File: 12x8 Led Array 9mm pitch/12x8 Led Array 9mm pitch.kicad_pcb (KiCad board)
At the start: 4 copper layers, 195 x 131.8 mm, 313 parts, among them J1 LED ch 1-24, J2 LED ch 25-48, J3 LED ch 49-72, J4 LED ch 73-96, J5 logic/analog, U1 CD74HC4067M96, U2 CD74HC4067M96, U3 CD74HC4067M96, U4 CD74HC4067M96, U5 CD74HC4067M96, U6 CD74HC4067M96

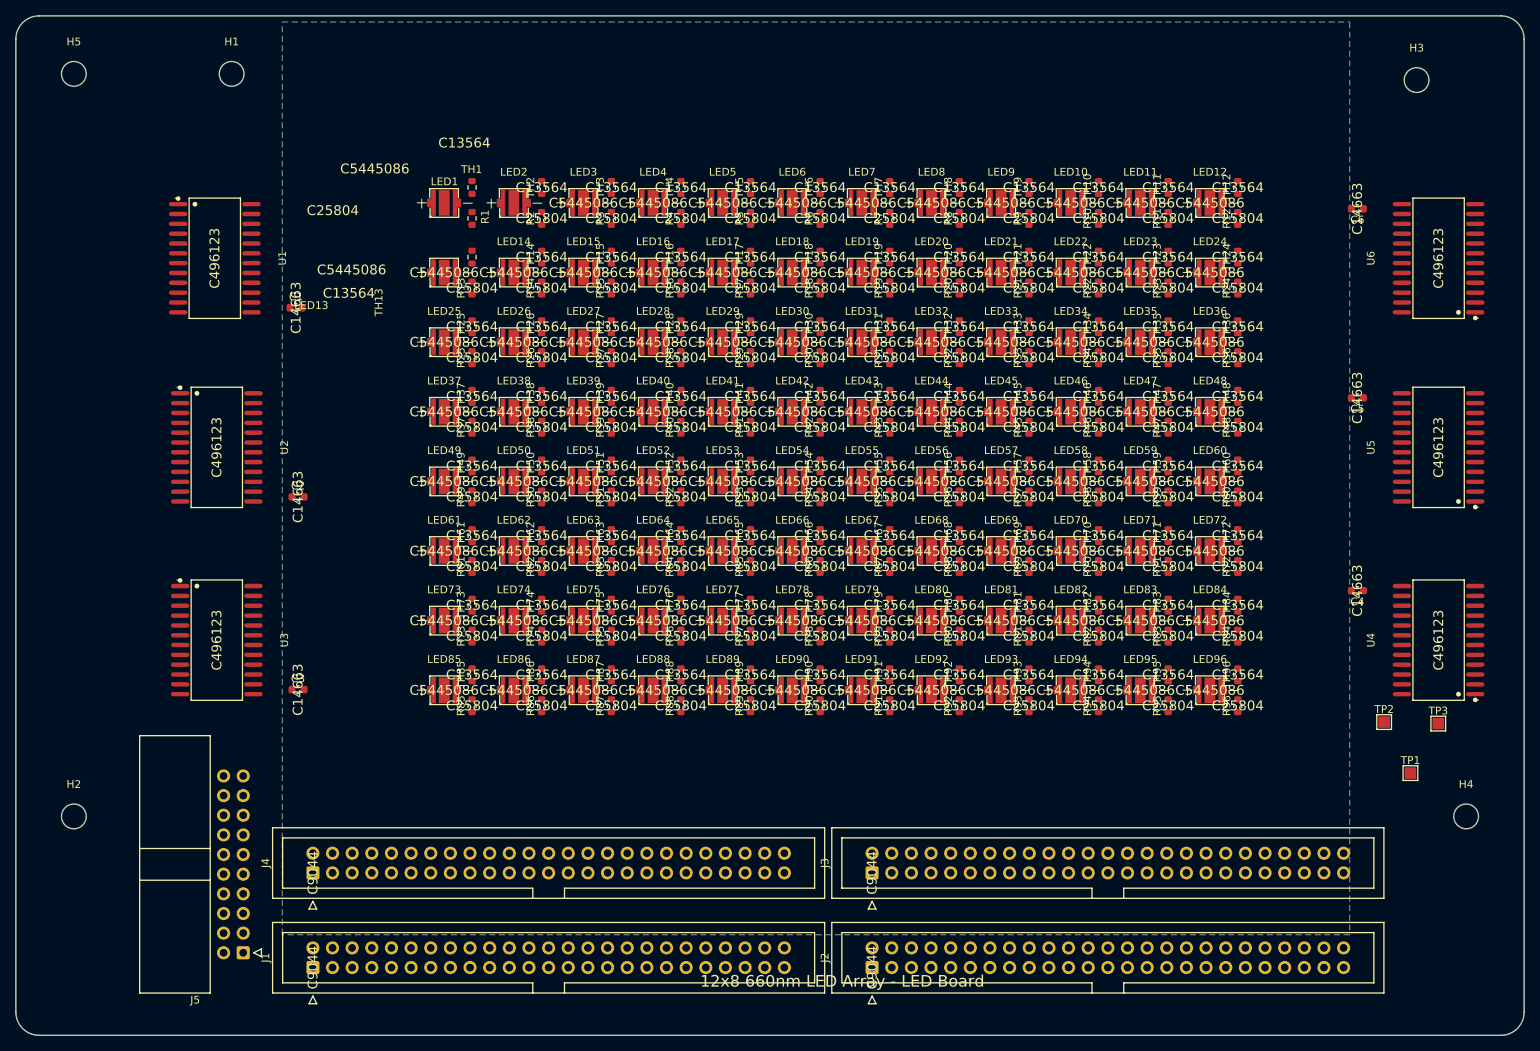
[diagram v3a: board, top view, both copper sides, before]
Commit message: Pull mux strips in (board now 190x131.8mm), thermal via farms + fills
- U1-U3/C1-C3 +5mm, U4-U6/C4-C6 -5mm; outline redrawn; H4 -> (227,128)
- 480 thermal vias (0.3/0.6mm, 5 per LED pad 3, cathode nets)
- 96 B.Cu cathode islands (6.5mm, solid connect, priority 2) + GND
  planes on In1/In2/B.Cu resized to new outline and filled
- PCB nets refreshed from the FIXED schematic netlist (board still
  carried the pre-fix merged +3.3V/GND net; GND net recreated,
  1051 pads re-netted, vias + zones re-assigned)

Co-Authored-By: Claude Fable 5 <noreply@anthropic.com>
Claude-Session: https://claude.ai/code/session_017oD54uh7Tvu54u9NPQNcZB
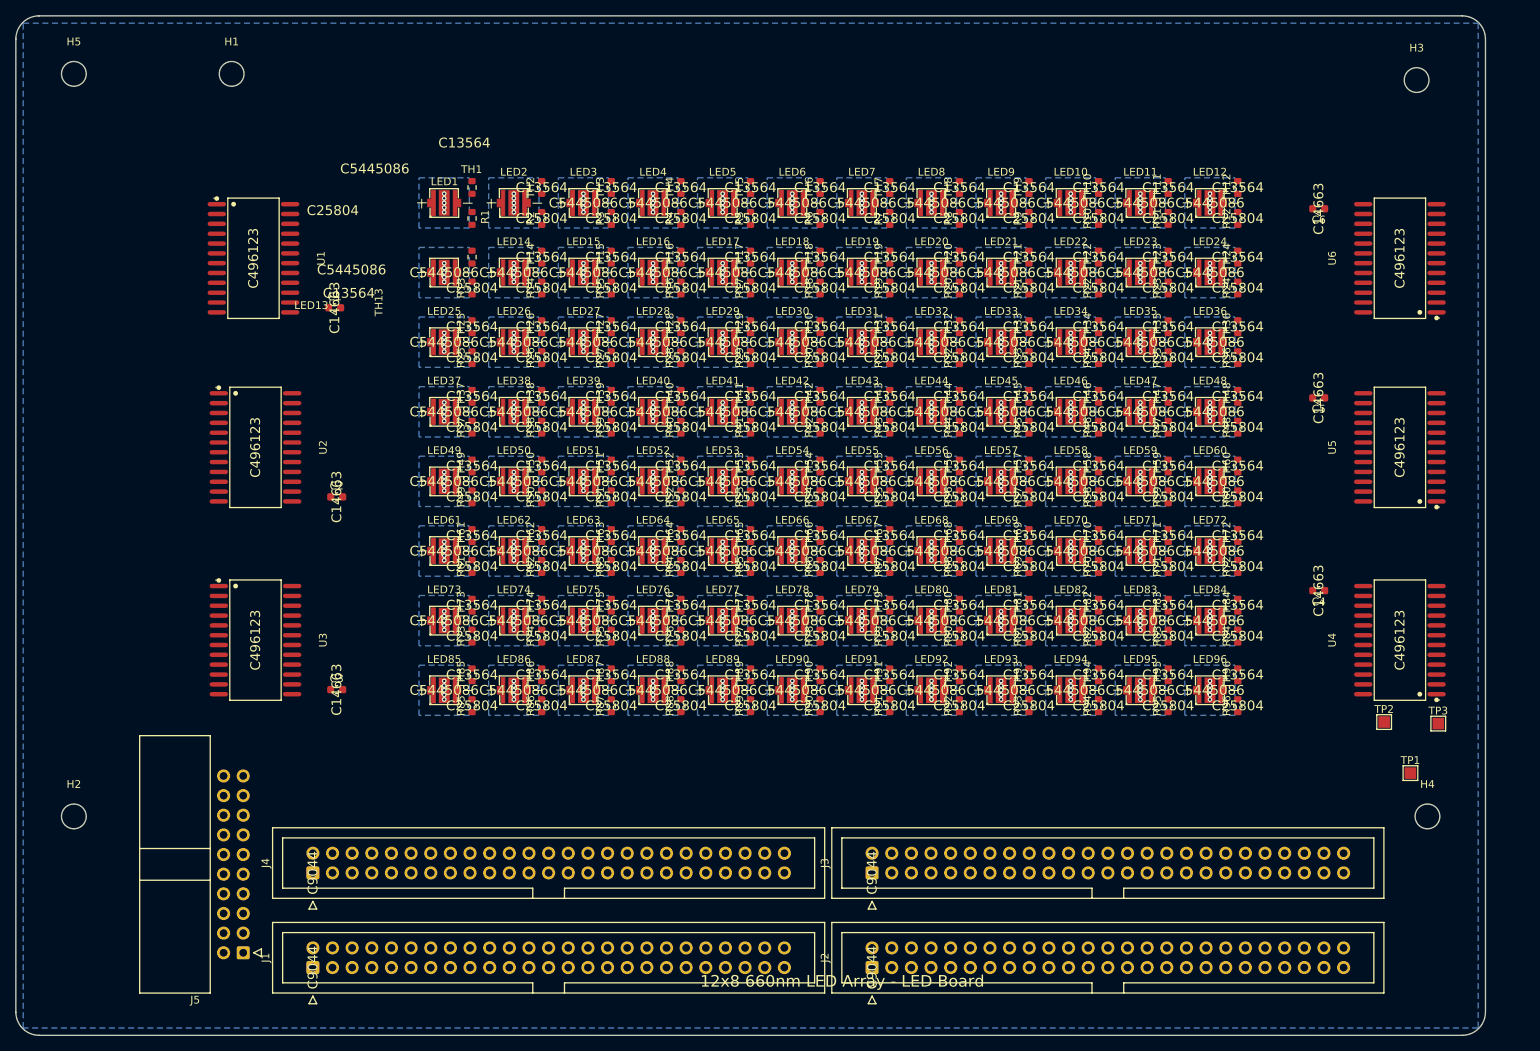
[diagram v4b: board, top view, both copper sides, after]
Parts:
- moved C1 5.00 mm to (85.7, 62.2)
- moved C2 5.00 mm to (86.0, 86.7)
- moved C3 5.00 mm to (86.0, 111.6)
- moved C4 5.00 mm to (212.9, 98.8)
- moved C5 5.00 mm to (212.9, 73.9)
- moved C6 5.00 mm to (212.9, 49.4)
- moved H4 5.00 mm to (227.0, 128.0)
- moved U1 5.00 mm to (75.2, 55.8)
- moved U2 5.00 mm to (75.5, 80.3)
- moved U3 5.00 mm to (75.5, 105.2)
- moved U4 5.00 mm to (223.4, 105.2)
- moved U5 5.00 mm to (223.4, 80.3)
- moved U6 5.00 mm to (223.4, 55.8)
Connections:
- C1 pad 2: +3.3V -> GND
- C2 pad 2: +3.3V -> GND
- C3 pad 2: +3.3V -> GND
- C4 pad 2: +3.3V -> GND
- C5 pad 2: +3.3V -> GND
- C6 pad 2: +3.3V -> GND
- J1 pad 10: /LED_K5 -> /LED_K2
- J1 pad 11: /LED_A6 -> /LED_A14
- J1 pad 12: /LED_K6 -> /LED_K14
- J1 pad 13: /LED_A7 -> /LED_A26
- J1 pad 14: /LED_K7 -> /LED_K26
- J1 pad 15: /LED_A8 -> /LED_A38
- J1 pad 16: /LED_K8 -> /LED_K38
- J1 pad 17: /LED_A9 -> /LED_A3
- J1 pad 18: /LED_K9 -> /LED_K3
- J1 pad 19: /LED_A10 -> /LED_A15
- J1 pad 20: /LED_K10 -> /LED_K15
- J1 pad 21: /LED_A11 -> /LED_A27
- J1 pad 22: /LED_K11 -> /LED_K27
- J1 pad 23: /LED_A12 -> /LED_A39
- J1 pad 24: /LED_K12 -> /LED_K39
- J1 pad 25: /LED_A13 -> /LED_A4
- J1 pad 26: /LED_K13 -> /LED_K4
- J1 pad 27: /LED_A14 -> /LED_A16
- J1 pad 28: /LED_K14 -> /LED_K16
- J1 pad 29: /LED_A15 -> /LED_A28
- J1 pad 3: /LED_A2 -> /LED_A13
- J1 pad 30: /LED_K15 -> /LED_K28
- J1 pad 31: /LED_A16 -> /LED_A40
- J1 pad 32: /LED_K16 -> /LED_K40
- J1 pad 33: /LED_A17 -> /LED_A5
- J1 pad 34: /LED_K17 -> /LED_K5
- J1 pad 35: /LED_A18 -> /LED_A17
- J1 pad 36: /LED_K18 -> /LED_K17
- J1 pad 37: /LED_A19 -> /LED_A29
- J1 pad 38: /LED_K19 -> /LED_K29
- J1 pad 39: /LED_A20 -> /LED_A41
- J1 pad 4: /LED_K2 -> /LED_K13
- J1 pad 40: /LED_K20 -> /LED_K41
- J1 pad 41: /LED_A21 -> /LED_A6
- J1 pad 42: /LED_K21 -> /LED_K6
- J1 pad 43: /LED_A22 -> /LED_A18
- J1 pad 44: /LED_K22 -> /LED_K18
- J1 pad 45: /LED_A23 -> /LED_A30
- J1 pad 46: /LED_K23 -> /LED_K30
- J1 pad 47: /LED_A24 -> /LED_A42
- J1 pad 48: /LED_K24 -> /LED_K42
- J1 pad 49: +3.3V -> GND
- J1 pad 5: /LED_A3 -> /LED_A25
- J1 pad 50: +3.3V -> GND
- J1 pad 6: /LED_K3 -> /LED_K25
- J1 pad 7: /LED_A4 -> /LED_A37
- J1 pad 8: /LED_K4 -> /LED_K37
- J1 pad 9: /LED_A5 -> /LED_A2
- J2 pad 1: /LED_A25 -> /LED_A7
- J2 pad 10: /LED_K29 -> /LED_K8
- J2 pad 11: /LED_A30 -> /LED_A20
- J2 pad 12: /LED_K30 -> /LED_K20
- J2 pad 13: /LED_A31 -> /LED_A32
- J2 pad 14: /LED_K31 -> /LED_K32
- J2 pad 15: /LED_A32 -> /LED_A44
- J2 pad 16: /LED_K32 -> /LED_K44
- J2 pad 17: /LED_A33 -> /LED_A9
- J2 pad 18: /LED_K33 -> /LED_K9
- J2 pad 19: /LED_A34 -> /LED_A21
- J2 pad 2: /LED_K25 -> /LED_K7
- J2 pad 20: /LED_K34 -> /LED_K21
- J2 pad 21: /LED_A35 -> /LED_A33
- J2 pad 22: /LED_K35 -> /LED_K33
- J2 pad 23: /LED_A36 -> /LED_A45
- J2 pad 24: /LED_K36 -> /LED_K45
- J2 pad 25: /LED_A37 -> /LED_A10
- J2 pad 26: /LED_K37 -> /LED_K10
- J2 pad 27: /LED_A38 -> /LED_A22
- J2 pad 28: /LED_K38 -> /LED_K22
- J2 pad 29: /LED_A39 -> /LED_A34
- J2 pad 3: /LED_A26 -> /LED_A19
- J2 pad 30: /LED_K39 -> /LED_K34
- J2 pad 31: /LED_A40 -> /LED_A46
- J2 pad 32: /LED_K40 -> /LED_K46
- J2 pad 33: /LED_A41 -> /LED_A11
- J2 pad 34: /LED_K41 -> /LED_K11
- J2 pad 35: /LED_A42 -> /LED_A23
- J2 pad 36: /LED_K42 -> /LED_K23
- J2 pad 37: /LED_A43 -> /LED_A35
- J2 pad 38: /LED_K43 -> /LED_K35
- J2 pad 39: /LED_A44 -> /LED_A47
- J2 pad 4: /LED_K26 -> /LED_K19
- J2 pad 40: /LED_K44 -> /LED_K47
- J2 pad 41: /LED_A45 -> /LED_A12
- J2 pad 42: /LED_K45 -> /LED_K12
- J2 pad 43: /LED_A46 -> /LED_A24
- J2 pad 44: /LED_K46 -> /LED_K24
- J2 pad 45: /LED_A47 -> /LED_A36
- J2 pad 46: /LED_K47 -> /LED_K36
- J2 pad 49: +3.3V -> GND
- J2 pad 5: /LED_A27 -> /LED_A31
- J2 pad 50: +3.3V -> GND
- J2 pad 6: /LED_K27 -> /LED_K31
- J2 pad 7: /LED_A28 -> /LED_A43
- J2 pad 8: /LED_K28 -> /LED_K43
- J2 pad 9: /LED_A29 -> /LED_A8
- J3 pad 1: /LED_A49 -> /LED_A55
- J3 pad 10: /LED_K53 -> /LED_K56
- J3 pad 11: /LED_A54 -> /LED_A68
- J3 pad 12: /LED_K54 -> /LED_K68
- J3 pad 13: /LED_A55 -> /LED_A80
- J3 pad 14: /LED_K55 -> /LED_K80
- J3 pad 15: /LED_A56 -> /LED_A92
- J3 pad 16: /LED_K56 -> /LED_K92
- J3 pad 19: /LED_A58 -> /LED_A69
- J3 pad 2: /LED_K49 -> /LED_K55
- J3 pad 20: /LED_K58 -> /LED_K69
- J3 pad 21: /LED_A59 -> /LED_A81
- J3 pad 22: /LED_K59 -> /LED_K81
- J3 pad 23: /LED_A60 -> /LED_A93
- J3 pad 24: /LED_K60 -> /LED_K93
- J3 pad 25: /LED_A61 -> /LED_A58
- J3 pad 26: /LED_K61 -> /LED_K58
- J3 pad 27: /LED_A62 -> /LED_A70
- J3 pad 28: /LED_K62 -> /LED_K70
- J3 pad 29: /LED_A63 -> /LED_A82
- J3 pad 3: /LED_A50 -> /LED_A67
- J3 pad 30: /LED_K63 -> /LED_K82
- J3 pad 31: /LED_A64 -> /LED_A94
- J3 pad 32: /LED_K64 -> /LED_K94
- J3 pad 33: /LED_A65 -> /LED_A59
- J3 pad 34: /LED_K65 -> /LED_K59
- J3 pad 35: /LED_A66 -> /LED_A71
- J3 pad 36: /LED_K66 -> /LED_K71
- J3 pad 37: /LED_A67 -> /LED_A83
- J3 pad 38: /LED_K67 -> /LED_K83
- J3 pad 39: /LED_A68 -> /LED_A95
- J3 pad 4: /LED_K50 -> /LED_K67
- J3 pad 40: /LED_K68 -> /LED_K95
- J3 pad 41: /LED_A69 -> /LED_A60
- J3 pad 42: /LED_K69 -> /LED_K60
- J3 pad 43: /LED_A70 -> /LED_A72
- J3 pad 44: /LED_K70 -> /LED_K72
- J3 pad 45: /LED_A71 -> /LED_A84
- J3 pad 46: /LED_K71 -> /LED_K84
- J3 pad 47: /LED_A72 -> /LED_A96
- J3 pad 48: /LED_K72 -> /LED_K96
- J3 pad 49: +3.3V -> GND
- J3 pad 5: /LED_A51 -> /LED_A79
- J3 pad 50: +3.3V -> GND
- J3 pad 6: /LED_K51 -> /LED_K79
- J3 pad 7: /LED_A52 -> /LED_A91
- J3 pad 8: /LED_K52 -> /LED_K91
- J3 pad 9: /LED_A53 -> /LED_A56
- J4 pad 1: /LED_A73 -> /LED_A49
- J4 pad 10: /LED_K77 -> /LED_K50
- J4 pad 11: /LED_A78 -> /LED_A62
- J4 pad 12: /LED_K78 -> /LED_K62
- J4 pad 13: /LED_A79 -> /LED_A74
- J4 pad 14: /LED_K79 -> /LED_K74
- J4 pad 15: /LED_A80 -> /LED_A86
- J4 pad 16: /LED_K80 -> /LED_K86
- J4 pad 17: /LED_A81 -> /LED_A51
- J4 pad 18: /LED_K81 -> /LED_K51
- J4 pad 19: /LED_A82 -> /LED_A63
- J4 pad 2: /LED_K73 -> /LED_K49
- J4 pad 20: /LED_K82 -> /LED_K63
- J4 pad 21: /LED_A83 -> /LED_A75
- J4 pad 22: /LED_K83 -> /LED_K75
- J4 pad 23: /LED_A84 -> /LED_A87
- J4 pad 24: /LED_K84 -> /LED_K87
- J4 pad 25: /LED_A85 -> /LED_A52
- J4 pad 26: /LED_K85 -> /LED_K52
- J4 pad 27: /LED_A86 -> /LED_A64
- J4 pad 28: /LED_K86 -> /LED_K64
- J4 pad 29: /LED_A87 -> /LED_A76
- J4 pad 3: /LED_A74 -> /LED_A61
- J4 pad 30: /LED_K87 -> /LED_K76
- J4 pad 33: /LED_A89 -> /LED_A53
- J4 pad 34: /LED_K89 -> /LED_K53
- J4 pad 35: /LED_A90 -> /LED_A65
- J4 pad 36: /LED_K90 -> /LED_K65
- J4 pad 37: /LED_A91 -> /LED_A77
- J4 pad 38: /LED_K91 -> /LED_K77
- J4 pad 39: /LED_A92 -> /LED_A89
- J4 pad 4: /LED_K74 -> /LED_K61
- J4 pad 40: /LED_K92 -> /LED_K89
- J4 pad 41: /LED_A93 -> /LED_A54
- J4 pad 42: /LED_K93 -> /LED_K54
- J4 pad 43: /LED_A94 -> /LED_A66
- J4 pad 44: /LED_K94 -> /LED_K66
- J4 pad 45: /LED_A95 -> /LED_A78
- J4 pad 46: /LED_K95 -> /LED_K78
- J4 pad 47: /LED_A96 -> /LED_A90
- J4 pad 48: /LED_K96 -> /LED_K90
- J4 pad 49: +3.3V -> GND
- J4 pad 5: /LED_A75 -> /LED_A73
- J4 pad 50: +3.3V -> GND
- J4 pad 6: /LED_K75 -> /LED_K73
- J4 pad 7: /LED_A76 -> /LED_A85
- J4 pad 8: /LED_K76 -> /LED_K85
- J4 pad 9: /LED_A77 -> /LED_A50
- J5 pad 10: +3.3V -> GND
- J5 pad 12: +3.3V -> GND
- J5 pad 14: +3.3V -> GND
- J5 pad 19: +3.3V -> GND
- J5 pad 2: +3.3V -> GND
- J5 pad 20: +3.3V -> GND
- J5 pad 4: +3.3V -> GND
- J5 pad 6: +3.3V -> GND
- J5 pad 8: +3.3V -> GND
- R1 pad 2: +3.3V -> GND
- R10 pad 2: +3.3V -> GND
- R11 pad 2: +3.3V -> GND
- R12 pad 2: +3.3V -> GND
- R13 pad 2: +3.3V -> GND
- R14 pad 2: +3.3V -> GND
- R15 pad 2: +3.3V -> GND
- R16 pad 2: +3.3V -> GND
- R17 pad 2: +3.3V -> GND
- R18 pad 2: +3.3V -> GND
- R19 pad 2: +3.3V -> GND
- R2 pad 2: +3.3V -> GND
- R20 pad 2: +3.3V -> GND
- R21 pad 2: +3.3V -> GND
- R22 pad 2: +3.3V -> GND
- R23 pad 2: +3.3V -> GND
- R24 pad 2: +3.3V -> GND
- R25 pad 2: +3.3V -> GND
- R26 pad 2: +3.3V -> GND
- R27 pad 2: +3.3V -> GND
- R28 pad 2: +3.3V -> GND
- R29 pad 2: +3.3V -> GND
- R3 pad 2: +3.3V -> GND
- R30 pad 2: +3.3V -> GND
- R31 pad 2: +3.3V -> GND
- R32 pad 2: +3.3V -> GND
- R33 pad 2: +3.3V -> GND
- R34 pad 2: +3.3V -> GND
- R35 pad 2: +3.3V -> GND
- R36 pad 2: +3.3V -> GND
- R37 pad 2: +3.3V -> GND
- R38 pad 2: +3.3V -> GND
- R39 pad 2: +3.3V -> GND
- R4 pad 2: +3.3V -> GND
- R40 pad 2: +3.3V -> GND
- R41 pad 2: +3.3V -> GND
- R42 pad 2: +3.3V -> GND
- R43 pad 2: +3.3V -> GND
- R44 pad 2: +3.3V -> GND
- R45 pad 2: +3.3V -> GND
- R46 pad 2: +3.3V -> GND
- R47 pad 2: +3.3V -> GND
- R48 pad 2: +3.3V -> GND
- R49 pad 2: +3.3V -> GND
- R5 pad 2: +3.3V -> GND
- R50 pad 2: +3.3V -> GND
- R51 pad 2: +3.3V -> GND
- R52 pad 2: +3.3V -> GND
- R53 pad 2: +3.3V -> GND
- R54 pad 2: +3.3V -> GND
- R55 pad 2: +3.3V -> GND
- R56 pad 2: +3.3V -> GND
- R57 pad 2: +3.3V -> GND
- R58 pad 2: +3.3V -> GND
- R59 pad 2: +3.3V -> GND
- R6 pad 2: +3.3V -> GND
- R60 pad 2: +3.3V -> GND
- R61 pad 2: +3.3V -> GND
- R62 pad 2: +3.3V -> GND
- R63 pad 2: +3.3V -> GND
- R64 pad 2: +3.3V -> GND
- R65 pad 2: +3.3V -> GND
- R66 pad 2: +3.3V -> GND
- R67 pad 2: +3.3V -> GND
- R68 pad 2: +3.3V -> GND
- R69 pad 2: +3.3V -> GND
- R7 pad 2: +3.3V -> GND
- R70 pad 2: +3.3V -> GND
- R71 pad 2: +3.3V -> GND
- R72 pad 2: +3.3V -> GND
- R73 pad 2: +3.3V -> GND
- R74 pad 2: +3.3V -> GND
- R75 pad 2: +3.3V -> GND
- R76 pad 2: +3.3V -> GND
- R77 pad 2: +3.3V -> GND
- R78 pad 2: +3.3V -> GND
- R79 pad 2: +3.3V -> GND
- R8 pad 2: +3.3V -> GND
- R80 pad 2: +3.3V -> GND
- R81 pad 2: +3.3V -> GND
- R82 pad 2: +3.3V -> GND
- R83 pad 2: +3.3V -> GND
- R84 pad 2: +3.3V -> GND
- R85 pad 2: +3.3V -> GND
- R86 pad 2: +3.3V -> GND
- R87 pad 2: +3.3V -> GND
- R88 pad 2: +3.3V -> GND
- R89 pad 2: +3.3V -> GND
- R9 pad 2: +3.3V -> GND
- R90 pad 2: +3.3V -> GND
- R91 pad 2: +3.3V -> GND
- R92 pad 2: +3.3V -> GND
- R93 pad 2: +3.3V -> GND
- R94 pad 2: +3.3V -> GND
- R95 pad 2: +3.3V -> GND
- R96 pad 2: +3.3V -> GND
- TH1 pad 1: +3V3 -> +3.3V
- TH10 pad 1: +3V3 -> +3.3V
- TH11 pad 1: +3V3 -> +3.3V
- TH12 pad 1: +3V3 -> +3.3V
- TH13 pad 1: +3V3 -> +3.3V
- TH14 pad 1: +3V3 -> +3.3V
- TH15 pad 1: +3V3 -> +3.3V
- TH16 pad 1: +3V3 -> +3.3V
- TH17 pad 1: +3V3 -> +3.3V
- TH18 pad 1: +3V3 -> +3.3V
- TH19 pad 1: +3V3 -> +3.3V
- TH2 pad 1: +3V3 -> +3.3V
- TH20 pad 1: +3V3 -> +3.3V
- TH21 pad 1: +3V3 -> +3.3V
- TH22 pad 1: +3V3 -> +3.3V
- TH23 pad 1: +3V3 -> +3.3V
- TH24 pad 1: +3V3 -> +3.3V
- TH25 pad 1: +3V3 -> +3.3V
- TH26 pad 1: +3V3 -> +3.3V
- TH27 pad 1: +3V3 -> +3.3V
- TH28 pad 1: +3V3 -> +3.3V
- TH29 pad 1: +3V3 -> +3.3V
- TH3 pad 1: +3V3 -> +3.3V
- TH30 pad 1: +3V3 -> +3.3V
- TH31 pad 1: +3V3 -> +3.3V
- TH32 pad 1: +3V3 -> +3.3V
- TH33 pad 1: +3V3 -> +3.3V
- TH34 pad 1: +3V3 -> +3.3V
- TH35 pad 1: +3V3 -> +3.3V
- TH36 pad 1: +3V3 -> +3.3V
- TH37 pad 1: +3V3 -> +3.3V
- TH38 pad 1: +3V3 -> +3.3V
- TH39 pad 1: +3V3 -> +3.3V
- TH4 pad 1: +3V3 -> +3.3V
- TH40 pad 1: +3V3 -> +3.3V
- TH41 pad 1: +3V3 -> +3.3V
- TH42 pad 1: +3V3 -> +3.3V
- TH43 pad 1: +3V3 -> +3.3V
- TH44 pad 1: +3V3 -> +3.3V
- TH45 pad 1: +3V3 -> +3.3V
- TH46 pad 1: +3V3 -> +3.3V
- TH47 pad 1: +3V3 -> +3.3V
- TH48 pad 1: +3V3 -> +3.3V
- TH49 pad 1: +3V3 -> +3.3V
- TH5 pad 1: +3V3 -> +3.3V
- TH50 pad 1: +3V3 -> +3.3V
- TH51 pad 1: +3V3 -> +3.3V
- TH52 pad 1: +3V3 -> +3.3V
- TH53 pad 1: +3V3 -> +3.3V
- TH54 pad 1: +3V3 -> +3.3V
- TH55 pad 1: +3V3 -> +3.3V
- TH56 pad 1: +3V3 -> +3.3V
- TH57 pad 1: +3V3 -> +3.3V
- TH58 pad 1: +3V3 -> +3.3V
- TH59 pad 1: +3V3 -> +3.3V
- TH6 pad 1: +3V3 -> +3.3V
- TH60 pad 1: +3V3 -> +3.3V
- TH61 pad 1: +3V3 -> +3.3V
- TH62 pad 1: +3V3 -> +3.3V
- TH63 pad 1: +3V3 -> +3.3V
- TH64 pad 1: +3V3 -> +3.3V
- TH65 pad 1: +3V3 -> +3.3V
- TH66 pad 1: +3V3 -> +3.3V
- TH67 pad 1: +3V3 -> +3.3V
- TH68 pad 1: +3V3 -> +3.3V
- TH69 pad 1: +3V3 -> +3.3V
- TH7 pad 1: +3V3 -> +3.3V
- TH70 pad 1: +3V3 -> +3.3V
- TH71 pad 1: +3V3 -> +3.3V
- TH72 pad 1: +3V3 -> +3.3V
- TH73 pad 1: +3V3 -> +3.3V
- TH74 pad 1: +3V3 -> +3.3V
- TH75 pad 1: +3V3 -> +3.3V
- TH76 pad 1: +3V3 -> +3.3V
- TH77 pad 1: +3V3 -> +3.3V
- TH78 pad 1: +3V3 -> +3.3V
- TH79 pad 1: +3V3 -> +3.3V
- TH8 pad 1: +3V3 -> +3.3V
- TH80 pad 1: +3V3 -> +3.3V
- TH81 pad 1: +3V3 -> +3.3V
- TH82 pad 1: +3V3 -> +3.3V
- TH83 pad 1: +3V3 -> +3.3V
- TH84 pad 1: +3V3 -> +3.3V
- TH85 pad 1: +3V3 -> +3.3V
- TH86 pad 1: +3V3 -> +3.3V
- TH87 pad 1: +3V3 -> +3.3V
- TH88 pad 1: +3V3 -> +3.3V
- TH89 pad 1: +3V3 -> +3.3V
- TH9 pad 1: +3V3 -> +3.3V
- TH90 pad 1: +3V3 -> +3.3V
- TH91 pad 1: +3V3 -> +3.3V
- TH92 pad 1: +3V3 -> +3.3V
- TH93 pad 1: +3V3 -> +3.3V
- TH94 pad 1: +3V3 -> +3.3V
- TH95 pad 1: +3V3 -> +3.3V
- TH96 pad 1: +3V3 -> +3.3V
- TP1 pad 1: +3V3 -> +3.3V
- TP2 pad 1: +3.3V -> GND
- TP3 pad 1: +3.3V -> GND
- U1 pad 12: +3.3V -> GND
- U1 pad 15: +3.3V -> GND
- U1 pad 16: /NTC16 -> /NTC28
- U1 pad 17: /NTC15 -> /NTC27
- U1 pad 18: /NTC14 -> /NTC26
- U1 pad 19: /NTC13 -> /NTC25
- U1 pad 2: /NTC8 -> /NTC14
- U1 pad 20: /NTC12 -> /NTC18
- U1 pad 21: /NTC11 -> /NTC17
- U1 pad 22: /NTC10 -> /NTC16
- U1 pad 23: /NTC9 -> /NTC15
- U1 pad 3: /NTC7 -> /NTC13
- U2 pad 12: +3.3V -> GND
- U2 pad 15: +3.3V -> GND
- U2 pad 16: /NTC32 -> /NTC62
- U2 pad 17: /NTC31 -> /NTC61
- U2 pad 18: /NTC30 -> /NTC54
- U2 pad 19: /NTC29 -> /NTC53
- U2 pad 2: /NTC24 -> /NTC42
- U2 pad 20: /NTC28 -> /NTC52
- U2 pad 21: /NTC27 -> /NTC51
- U2 pad 22: /NTC26 -> /NTC50
- U2 pad 23: /NTC25 -> /NTC49
- U2 pad 3: /NTC23 -> /NTC41
- U2 pad 4: /NTC22 -> /NTC40
- U2 pad 5: /NTC21 -> /NTC39
- U2 pad 6: /NTC20 -> /NTC38
- U2 pad 7: /NTC19 -> /NTC37
- U2 pad 8: /NTC18 -> /NTC30
- U2 pad 9: /NTC17 -> /NTC29
- U3 pad 12: +3.3V -> GND
- U3 pad 15: +3.3V -> GND
- U3 pad 16: /NTC48 -> /NTC90
- U3 pad 17: /NTC47 -> /NTC89
- U3 pad 18: /NTC46 -> /NTC88
- U3 pad 19: /NTC45 -> /NTC87
- U3 pad 2: /NTC40 -> /NTC76
- U3 pad 20: /NTC44 -> /NTC86
- U3 pad 21: /NTC43 -> /NTC85
- U3 pad 22: /NTC42 -> /NTC78
- U3 pad 23: /NTC41 -> /NTC77
- U3 pad 3: /NTC39 -> /NTC75
- U3 pad 4: /NTC38 -> /NTC74
- U3 pad 5: /NTC37 -> /NTC73
- U3 pad 6: /NTC36 -> /NTC66
- U3 pad 7: /NTC35 -> /NTC65
- U3 pad 8: /NTC34 -> /NTC64
- U3 pad 9: /NTC33 -> /NTC63
- U4 pad 12: +3.3V -> GND
- U4 pad 15: +3.3V -> GND
- U4 pad 16: /NTC64 -> /NTC96
- U4 pad 17: /NTC63 -> /NTC95
- U4 pad 18: /NTC62 -> /NTC94
- U4 pad 19: /NTC61 -> /NTC93
- U4 pad 2: /NTC56 -> /NTC82
- U4 pad 20: /NTC60 -> /NTC92
- U4 pad 21: /NTC59 -> /NTC91
- U4 pad 22: /NTC58 -> /NTC84
- U4 pad 23: /NTC57 -> /NTC83
- U4 pad 3: /NTC55 -> /NTC81
- U4 pad 4: /NTC54 -> /NTC80
- U4 pad 5: /NTC53 -> /NTC79
- U4 pad 6: /NTC52 -> /NTC72
- U4 pad 7: /NTC51 -> /NTC71
- U4 pad 8: /NTC50 -> /NTC70
- U4 pad 9: /NTC49 -> /NTC69
- U5 pad 12: +3.3V -> GND
- U5 pad 15: +3.3V -> GND
- U5 pad 16: /NTC80 -> /NTC68
- U5 pad 17: /NTC79 -> /NTC67
- U5 pad 18: /NTC78 -> /NTC60
- U5 pad 19: /NTC77 -> /NTC59
- U5 pad 2: /NTC72 -> /NTC48
- U5 pad 20: /NTC76 -> /NTC58
- U5 pad 21: /NTC75 -> /NTC57
- U5 pad 22: /NTC74 -> /NTC56
- U5 pad 23: /NTC73 -> /NTC55
- U5 pad 3: /NTC71 -> /NTC47
- U5 pad 4: /NTC70 -> /NTC46
- U5 pad 5: /NTC69 -> /NTC45
- U5 pad 6: /NTC68 -> /NTC44
- U5 pad 7: /NTC67 -> /NTC43
- U5 pad 8: /NTC66 -> /NTC36
- U5 pad 9: /NTC65 -> /NTC35
- U6 pad 12: +3.3V -> GND
- U6 pad 15: +3.3V -> GND
- U6 pad 16: /NTC96 -> /NTC34
- U6 pad 17: /NTC95 -> /NTC33
- U6 pad 18: /NTC94 -> /NTC32
- U6 pad 19: /NTC93 -> /NTC31
- U6 pad 2: /NTC88 -> /NTC20
- U6 pad 20: /NTC92 -> /NTC24
- U6 pad 21: /NTC91 -> /NTC23
- U6 pad 22: /NTC90 -> /NTC22
- U6 pad 23: /NTC89 -> /NTC21
- U6 pad 3: /NTC87 -> /NTC19
- U6 pad 4: /NTC86 -> /NTC12
- U6 pad 5: /NTC85 -> /NTC11
- U6 pad 6: /NTC84 -> /NTC10
- U6 pad 7: /NTC83 -> /NTC9
- U6 pad 8: /NTC82 -> /NTC8
- U6 pad 9: /NTC81 -> /NTC7
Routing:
- net /LED_K96: vias 0 -> 5
- net /LED_K95: vias 0 -> 5
- net /LED_K94: vias 0 -> 5
- net /LED_K93: vias 0 -> 5
- net /LED_K92: vias 0 -> 5
- net /LED_K91: vias 0 -> 5
- net /LED_K90: vias 0 -> 5
- net /LED_K9: vias 0 -> 5
- net /LED_K89: vias 0 -> 5
- net /LED_K88: vias 0 -> 5
- net /LED_K87: vias 0 -> 5
- net /LED_K86: vias 0 -> 5
- net /LED_K85: vias 0 -> 5
- net /LED_K84: vias 0 -> 5
- net /LED_K83: vias 0 -> 5
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- added copper zone on B.Cu, net /LED_K1
- added copper zone on B.Cu, net /LED_K10
- added copper zone on B.Cu, net /LED_K11
- added copper zone on B.Cu, net /LED_K12
- added copper zone on B.Cu, net /LED_K13
- added copper zone on B.Cu, net /LED_K14
- added copper zone on B.Cu, net /LED_K15
- added copper zone on B.Cu, net /LED_K16
- added copper zone on B.Cu, net /LED_K17
- added copper zone on B.Cu, net /LED_K18
- added copper zone on B.Cu, net /LED_K19
- added copper zone on B.Cu, net /LED_K2
- added copper zone on B.Cu, net /LED_K20
- added copper zone on B.Cu, net /LED_K21
- added copper zone on B.Cu, net /LED_K22
- added copper zone on B.Cu, net /LED_K23
- added copper zone on B.Cu, net /LED_K24
- added copper zone on B.Cu, net /LED_K25
- added copper zone on B.Cu, net /LED_K26
- added copper zone on B.Cu, net /LED_K27
- added copper zone on B.Cu, net /LED_K28
- added copper zone on B.Cu, net /LED_K29
- added copper zone on B.Cu, net /LED_K3
- added copper zone on B.Cu, net /LED_K30
- added copper zone on B.Cu, net /LED_K31
- added copper zone on B.Cu, net /LED_K32
- added copper zone on B.Cu, net /LED_K33
- added copper zone on B.Cu, net /LED_K34
- added copper zone on B.Cu, net /LED_K35
- added copper zone on B.Cu, net /LED_K36
- added copper zone on B.Cu, net /LED_K37
- added copper zone on B.Cu, net /LED_K38
- added copper zone on B.Cu, net /LED_K39
- added copper zone on B.Cu, net /LED_K4
- added copper zone on B.Cu, net /LED_K40
- added copper zone on B.Cu, net /LED_K41
- added copper zone on B.Cu, net /LED_K42
- added copper zone on B.Cu, net /LED_K43
- added copper zone on B.Cu, net /LED_K44
- added copper zone on B.Cu, net /LED_K45
- added copper zone on B.Cu, net /LED_K46
- added copper zone on B.Cu, net /LED_K47
- added copper zone on B.Cu, net /LED_K48
- added copper zone on B.Cu, net /LED_K49
- added copper zone on B.Cu, net /LED_K5
- added copper zone on B.Cu, net /LED_K50
- added copper zone on B.Cu, net /LED_K51
- added copper zone on B.Cu, net /LED_K52
- added copper zone on B.Cu, net /LED_K53
- added copper zone on B.Cu, net /LED_K54
- added copper zone on B.Cu, net /LED_K55
- added copper zone on B.Cu, net /LED_K56
- added copper zone on B.Cu, net /LED_K57
- added copper zone on B.Cu, net /LED_K58
- added copper zone on B.Cu, net /LED_K59
- added copper zone on B.Cu, net /LED_K6
- added copper zone on B.Cu, net /LED_K60
- added copper zone on B.Cu, net /LED_K61
- added copper zone on B.Cu, net /LED_K62
- added copper zone on B.Cu, net /LED_K63
- added copper zone on B.Cu, net /LED_K64
- added copper zone on B.Cu, net /LED_K65
- added copper zone on B.Cu, net /LED_K66
- added copper zone on B.Cu, net /LED_K67
- added copper zone on B.Cu, net /LED_K68
- added copper zone on B.Cu, net /LED_K69
- added copper zone on B.Cu, net /LED_K7
- added copper zone on B.Cu, net /LED_K70
- added copper zone on B.Cu, net /LED_K71
- added copper zone on B.Cu, net /LED_K72
- added copper zone on B.Cu, net /LED_K73
- added copper zone on B.Cu, net /LED_K74
- added copper zone on B.Cu, net /LED_K75
- added copper zone on B.Cu, net /LED_K76
- added copper zone on B.Cu, net /LED_K77
- added copper zone on B.Cu, net /LED_K78
- added copper zone on B.Cu, net /LED_K79
- added copper zone on B.Cu, net /LED_K8
- added copper zone on B.Cu, net /LED_K80
- added copper zone on B.Cu, net /LED_K81
- added copper zone on B.Cu, net /LED_K82
- added copper zone on B.Cu, net /LED_K83
- added copper zone on B.Cu, net /LED_K84
- added copper zone on B.Cu, net /LED_K85
- added copper zone on B.Cu, net /LED_K86
- added copper zone on B.Cu, net /LED_K87
- added copper zone on B.Cu, net /LED_K88
- added copper zone on B.Cu, net /LED_K89
- added copper zone on B.Cu, net /LED_K9
- added copper zone on B.Cu, net /LED_K90
- added copper zone on B.Cu, net /LED_K91
- added copper zone on B.Cu, net /LED_K92
- added copper zone on B.Cu, net /LED_K93
- added copper zone on B.Cu, net /LED_K94
- added copper zone on B.Cu, net /LED_K95
- added copper zone on B.Cu, net /LED_K96
- added copper zone on B.Cu, net GND
- added copper zone on In1.Cu, net GND
- added copper zone on In2.Cu, net GND
- removed copper zone on B.Cu, net (none)
- removed copper zone on In1.Cu, net (none)
- removed copper zone on In2.Cu, net (none)
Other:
- board size 195 x 131.8 mm -> 190 x 131.8 mm
